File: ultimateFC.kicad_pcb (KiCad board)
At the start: 6 copper layers, 36 x 36 mm, 240 parts, among them J1 USB_B_Micro, SW1 SW_Push, U1 LMR33630CQRNX, U2 TPS62824ADMQ, U3 LMR33620CRNXT, U4 S25FL064L, U5 DPS310, U6 BMI270, U7 STM32H735VGH6, U8 ICM-20602, Y1 CSTNE8M00G550000R0

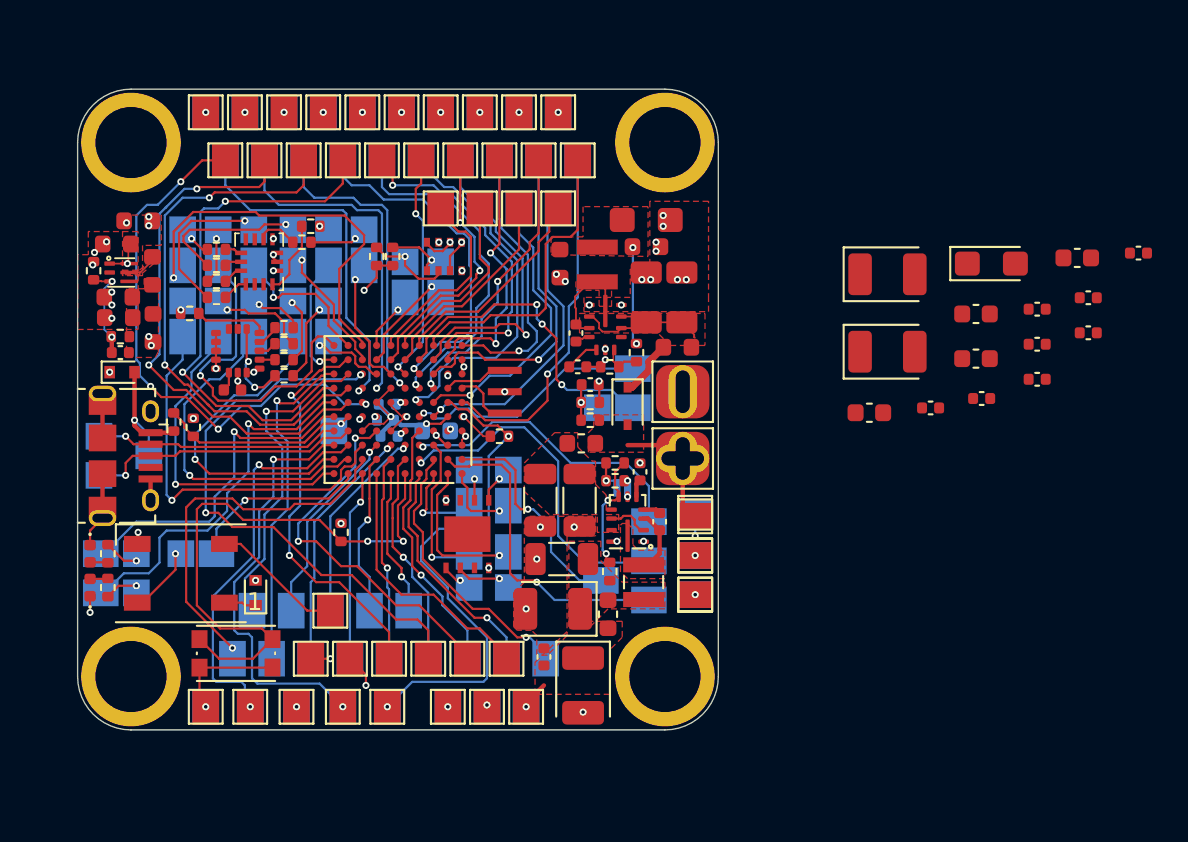
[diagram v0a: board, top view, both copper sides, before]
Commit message: add RF connectors
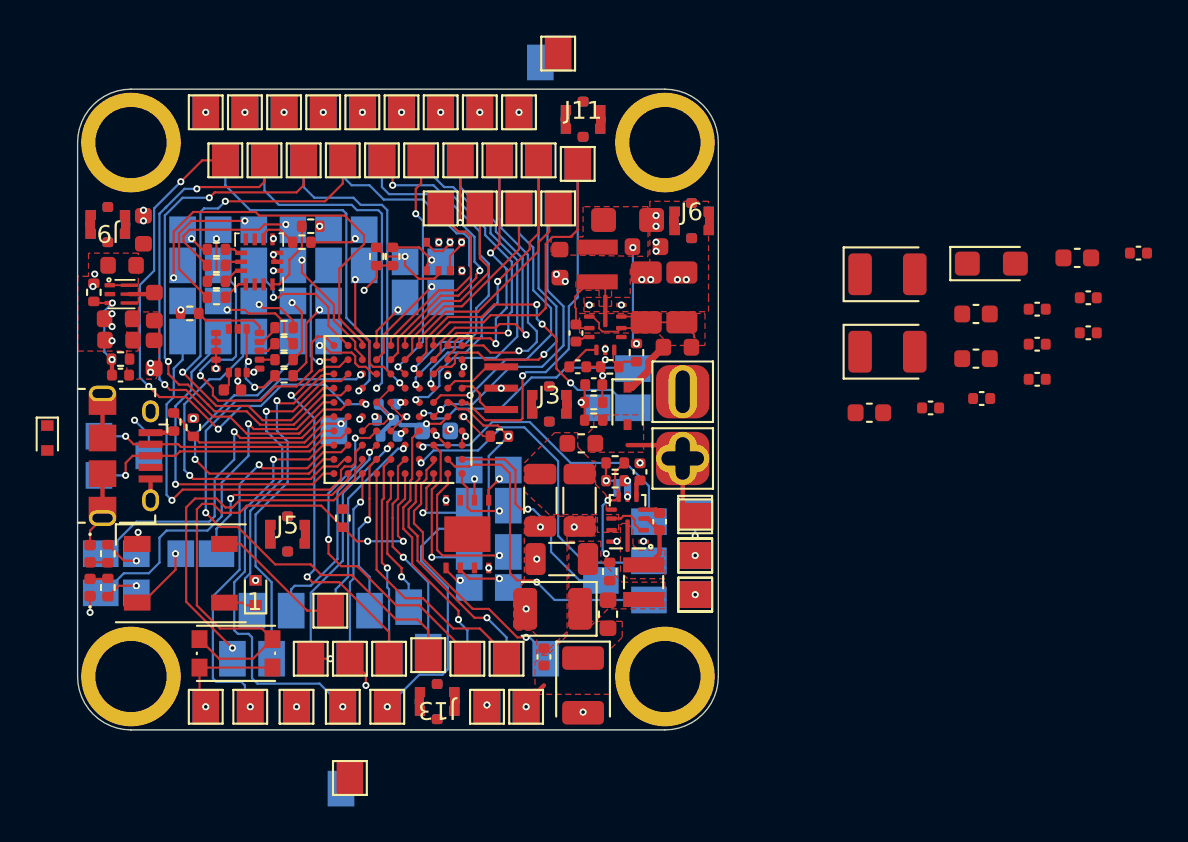
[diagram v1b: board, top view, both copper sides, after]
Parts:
- added J10: Conn_Coaxial, ultimateFC:Amphenol_RF_A-4JA, B.Cu at (125.4, 98.7)
- added J11: Conn_Coaxial, ultimateFC:Amphenol_RF_A-4JA, F.Cu at (125.4, 98.7)
- added J12: Conn_Coaxial, ultimateFC:Amphenol_RF_A-4JA, B.Cu at (117.2, 131.4)
- added J13: Conn_Coaxial, ultimateFC:Amphenol_RF_A-4JA, F.Cu at (117.2, 131.4)
- added J2: Conn_Coaxial, ultimateFC:Amphenol_RF_A-4JA, B.Cu at (123.5, 114.7)
- added J3: Conn_Coaxial, ultimateFC:Amphenol_RF_A-4JA, F.Cu at (123.5, 114.7)
- added J4: Conn_Coaxial, ultimateFC:Amphenol_RF_A-4JA, B.Cu at (108.8, 122.0)
- added J5: Conn_Coaxial, ultimateFC:Amphenol_RF_A-4JA, F.Cu at (108.8, 122.0)
- added J6: Conn_Coaxial, ultimateFC:Amphenol_RF_A-4JA, F.Cu at (131.5, 104.4)
- added J7: Conn_Coaxial, ultimateFC:Amphenol_RF_A-4JA, B.Cu at (131.5, 104.4)
- added J8: Conn_Coaxial, ultimateFC:Amphenol_RF_A-4JA, B.Cu at (98.7, 104.6)
- added J9: Conn_Coaxial, ultimateFC:Amphenol_RF_A-4JA, F.Cu at (98.7, 104.6)
- moved TP142 7.56 mm to (111.8, 136.3)
- moved TP28 6.80 mm to (112.3, 135.7)
- moved D4 5.60 mm to (95.3, 116.6), turned to -90 degrees
- moved TP126 3.30 mm to (124.0, 95.0)
- moved TP130 2.97 mm to (123.0, 95.5)
- moved L2 2.01 mm to (101.3, 109.2)
- moved FB4 1.49 mm to (101.3, 111.9)
- moved C26 1.27 mm to (99.3, 111.1)
- moved C23 1.27 mm to (99.4, 113.1)
- moved R3 1.27 mm to (99.4, 112.2)
- moved C11 1.24 mm to (99.5, 106.9)
- moved C24 1.22 mm to (99.3, 109.9)
- moved R4 1.22 mm to (97.9, 108.4)
- moved U2 1.22 mm to (99.5, 108.5)
- moved C6 1.05 mm to (127.9, 104.3)
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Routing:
- net USB_VBUS: track 7.73 -> 3.67 mm
- net /NRST: track 29.1 -> 25.7 mm
- net UART2_TX: track 20.9 -> 18.9 mm
- net Net-(C11-Pad1): track 1.96 -> 1.06 mm, vias 2 -> 0
- net ESC_4_TX: track 19.1 -> 19.8 mm
- net GND: track 19.5 -> 18.9 mm, vias 54 -> 51
- net Net-(TP51-Pad1): track 10.3 -> 10.8 mm
- net Net-(TP49-Pad1): track 11.3 -> 11.8 mm
- net +5V: vias 12 -> 10
- removed copper zone on F.Cu, net Net-(C11-Pad1)
- removed copper zone on F.Cu, net Net-(L2-Pad1)

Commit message: update layout
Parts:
- removed C10, C12, C13, C14, C15, C16, C17, C9: 4.7µF, Capacitor_SMD:C_0402_1005Metric
- removed C18, C19, C20, C21: 2.2µF, Capacitor_SMD:C_0603_1608Metric
- removed C22: 10µF, Capacitor_Tantalum_SMD:CP_EIA-3216-18_Kemet-A
- removed C7, C8: 220µF, Capacitor_Tantalum_SMD:CP_EIA-3528-15_AVX-H
- removed J10, J11, J12, J13, J6, J7: Conn_Coaxial, ultimateFC:Amphenol_RF_A-4JA
- moved J8 32.7 mm to (131.4, 104.6), turned to -90 degrees
- moved J9 32.7 mm to (131.4, 104.6), turned to 90 degrees
- moved TP142 7.56 mm to (117.8, 131.7)
- moved TP28 6.80 mm to (117.8, 131.7)
- moved D4 5.37 mm to (99.1, 112.8), turned to 0 degrees
- moved TP126 3.30 mm to (124.0, 98.3)
- moved TP130 2.97 mm to (124.0, 98.3)
- moved R11 2.22 mm to (113.2, 122.9), turned to -90 degrees
- moved C11 1.40 mm to (99.5, 105.5)
- moved C24 1.40 mm to (99.3, 108.5)
- moved FB4 1.40 mm to (101.3, 110.5)
- moved L2 1.40 mm to (101.3, 107.8)
- moved R3 1.40 mm to (99.4, 110.8)
- moved R4 1.40 mm to (97.9, 107.0)
- moved U2 1.40 mm to (99.5, 107.1)
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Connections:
- J4 pad 1: Net-(J5-Pad1) -> +5V
- J5 pad 1: Net-(J5-Pad1) -> +5V
- J8 pad 1: Net-(J8-Pad1) -> +3V3
- J9 pad 1: Net-(J8-Pad1) -> +3V3
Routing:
- net USB_VBUS: track 3.67 -> 7.01 mm
- net UART2_TX: track 18.9 -> 20.7 mm
- net UC_LED_1: track 18.7 -> 19.5 mm
- net Net-(TP75-Pad1): track 19.2 -> 18.5 mm
- net UART4_TX: track 16.0 -> 15.4 mm
- net Net-(TP74-Pad1): track 19.4 -> 18.8 mm
- net GND: track 18.9 -> 18.8 mm, vias 51 -> 62
- net Net-(J2-Pad1): vias 0 -> 1
- net +5V: vias 10 -> 13
- net +3V3: vias 18 -> 19
- added copper zone on F.Cu, net Net-(C11-Pad1)

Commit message: update layout
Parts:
- removed TP137, TP138, TP139, TP140, TP66: Pad, TestPoint:TestPoint_Pad_1.5x1.5mm
- added C39: 4.7µF, Capacitor_SMD:C_0603_1608Metric, F.Cu at (107.0, 125.1)
- SW1: footprint Button_Switch_SMD:SW_Push_1P1T_NO_CK_KMR2 -> Button_Switch_SMD:SW_Push_1P1T-SH_NO_CK_KMR2xxG
- TP141, TP65, TP67, TP88, TP89: footprint TestPoint:TestPoint_Pad_1.5x1.5mm -> ultimateFC:chonker_swd_pad
- moved D6 1.43 mm to (108.4, 125.6)
- moved R17 1.32 mm to (109.8, 104.3)
- moved R7 1.02 mm to (114.8, 106.6), turned to -90 degrees
- moved R8 1.02 mm to (115.7, 106.6), turned to -90 degrees
- moved R16 0.85 mm to (109.8, 105.5)
- moved D4 0.80 mm to (98.3, 112.8)
- moved J4 0.50 mm to (108.5, 122.4)
- moved J5 0.50 mm to (108.5, 122.4)
- moved SW1 0.40 mm to (105.9, 128.3)
- moved C27 0.32 mm to (125.1, 120.4)
- moved C28 0.30 mm to (123.0, 120.4)
- moved TP116 0.30 mm to (112.3, 128.7)
- moved TP36 0.30 mm to (114.5, 128.7)
- moved TP39 0.30 mm to (118.9, 128.7)
- moved TP40 0.30 mm to (116.7, 128.7)
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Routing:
- net UART3_RX: track 31.8 -> 36.1 mm
- net Net-(R11-Pad1): track 32.5 -> 28.7 mm
- net Net-(TP102-Pad1): track 17.9 -> 20.3 mm
- net /INT2_270: track 2.57 -> 4.70 mm
- net /SCL_DPS: track 4.82 -> 2.81 mm
- net Net-(TP50-Pad1): track 20.4 -> 22.4 mm
- net CS_OSD: track 21.6 -> 20.0 mm
- net /SCK_DPS: track 3.21 -> 1.68 mm
- net Net-(D5-Pad1): track 1.81 -> 3.34 mm
- net SCLK_GYRO: track 19.5 -> 20.8 mm
- net Net-(R16-Pad2): track 4.18 -> 3.24 mm
- net MISO_GYRO: track 19.3 -> 20.2 mm
- net MOSI_GYRO: track 18.4 -> 19.3 mm
- net Net-(TP49-Pad1): track 11.8 -> 11.0 mm
- net SCLK_OSD: track 7.01 -> 6.18 mm
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
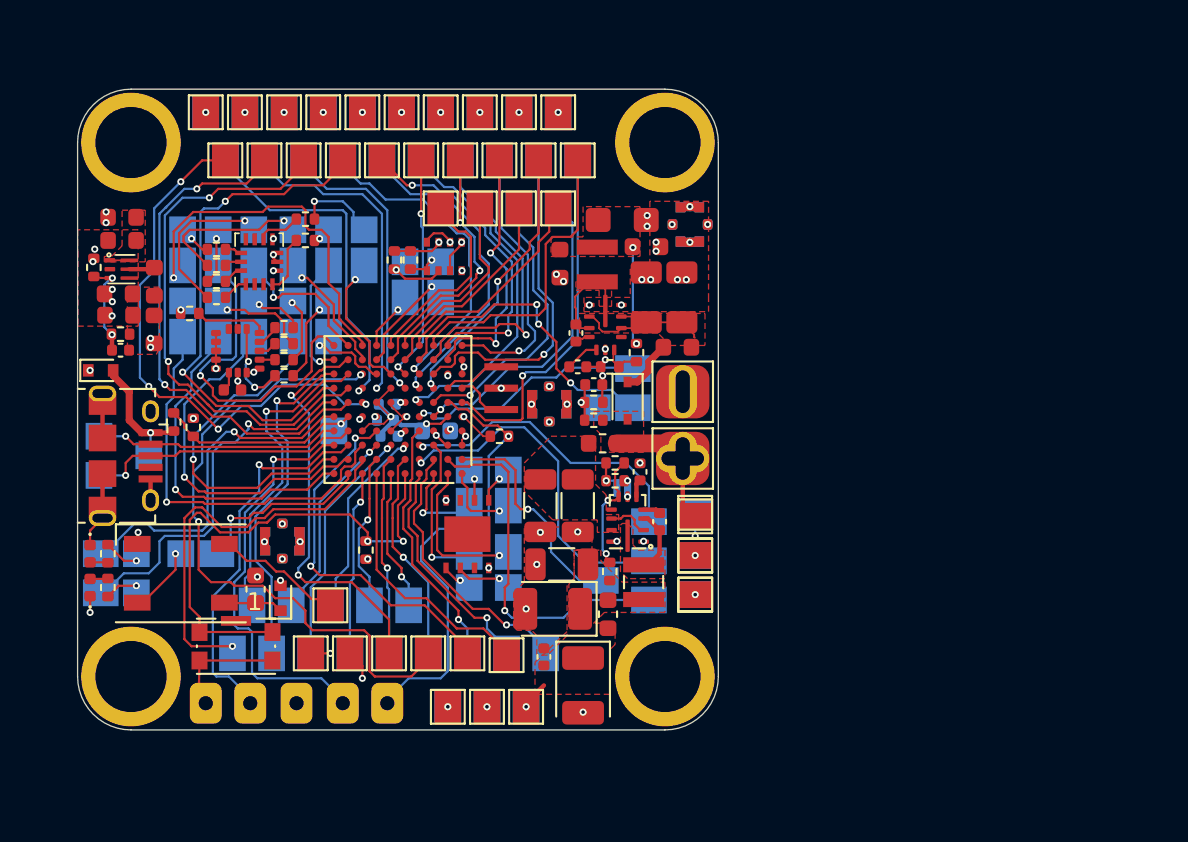
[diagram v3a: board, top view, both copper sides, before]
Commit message: change pads, add coax datasheet
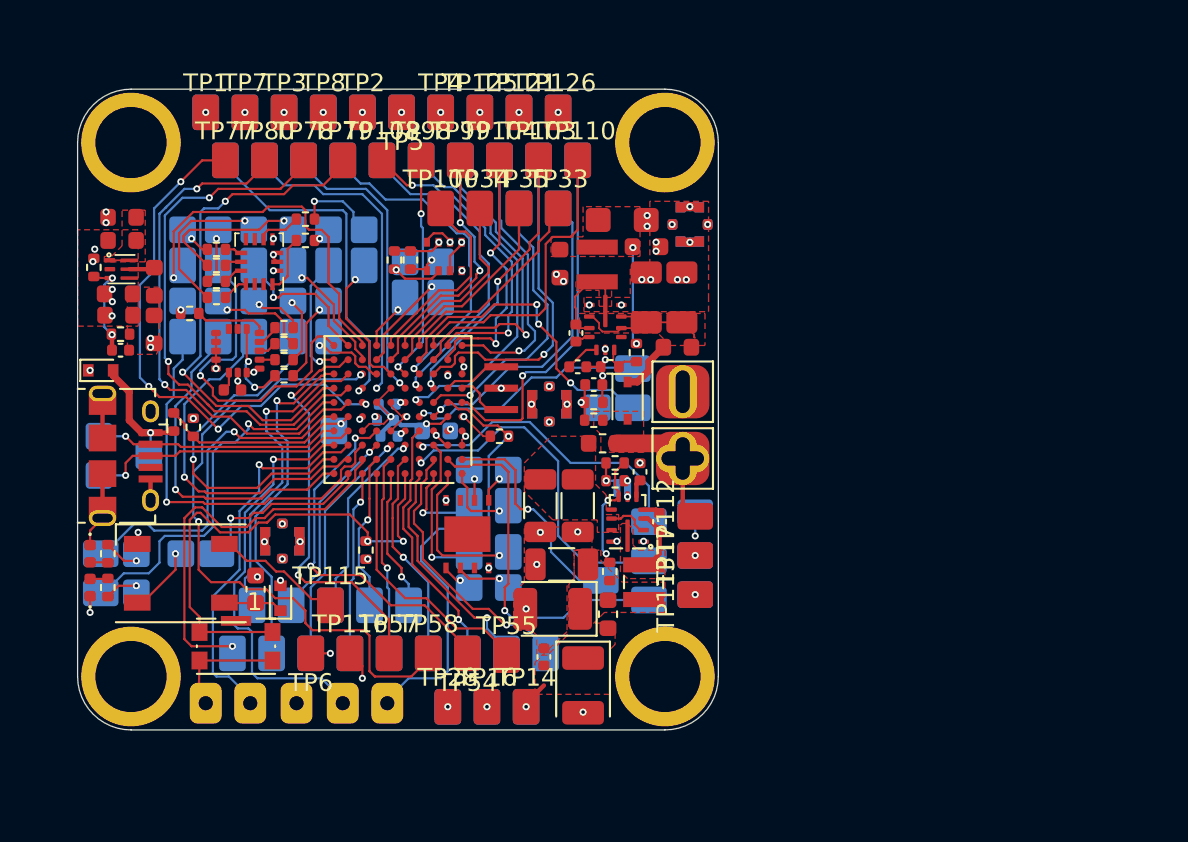
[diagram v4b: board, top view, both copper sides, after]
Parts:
- TP1, TP100, TP101, TP102, TP103, TP104, TP105, TP106, TP107, TP108, TP109, TP110, TP112, TP113, TP115, TP116, TP121, TP122, TP123, TP124, TP125, TP126, TP127, TP128, TP129, TP130, TP131, TP132, TP133, TP14, TP142, TP143, TP15, TP16, TP17, TP2, TP28, TP3, TP33, TP34, TP35, TP36, TP37, TP38, TP39, TP4, TP40, TP41, TP42, TP43, TP44, TP45, TP46, TP47, TP48, TP49, TP5, TP50, TP51, TP52, TP53, TP54, TP55, TP56, TP57, TP58, TP59, TP6, TP60, TP61, TP62, TP63, TP64, TP7, TP71, TP72, TP73, TP74, TP75, TP76, TP77, TP78, TP79, TP8, TP80, TP81, TP82, TP83, TP84, TP85, TP86, TP87, TP90, TP91, TP92, TP93, TP94, TP95, TP96, TP97, TP98, TP99: footprint TestPoint:TestPoint_Pad_1.5x1.5mm -> ultimateFC:chonker_TestPoint_Pad_1.5x2.0mm
- TP10, TP11, TP114, TP117, TP118, TP119, TP12, TP120, TP13, TP18, TP19, TP22, TP23, TP24, TP25, TP26, TP27, TP29, TP30, TP31, TP32, TP68, TP69, TP70, TP9: footprint TestPoint:TestPoint_Pad_1.5x1.5mm -> ultimateFC:chonker_TestPoint_Pad_1.5x1.5mm
- TP134, TP135, TP136: footprint TestPoint:TestPoint_Pad_1.5x1.5mm -> ultimateFC:chonker_TestPoint_Pad_1.5x2.0mm; moved to B.Cu

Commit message: update layout
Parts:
- TP141: moved to F.Cu
- TP65, TP67, TP88, TP89: moved to B.Cu
- turned TP141 to 0 degrees
- turned TP65 to 180 degrees
- turned TP67 to 180 degrees
- turned TP88 to 180 degrees
- turned TP89 to 180 degrees

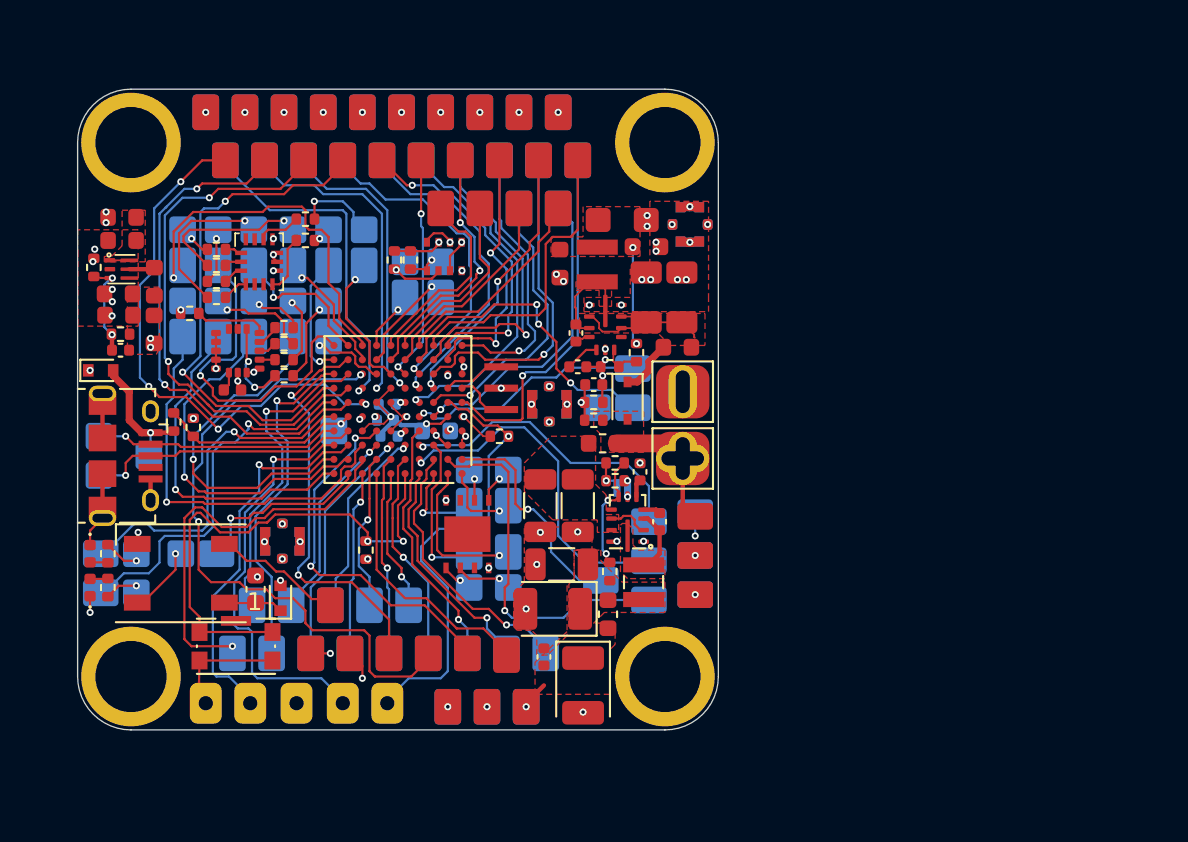
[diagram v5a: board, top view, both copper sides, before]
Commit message: Added Caps
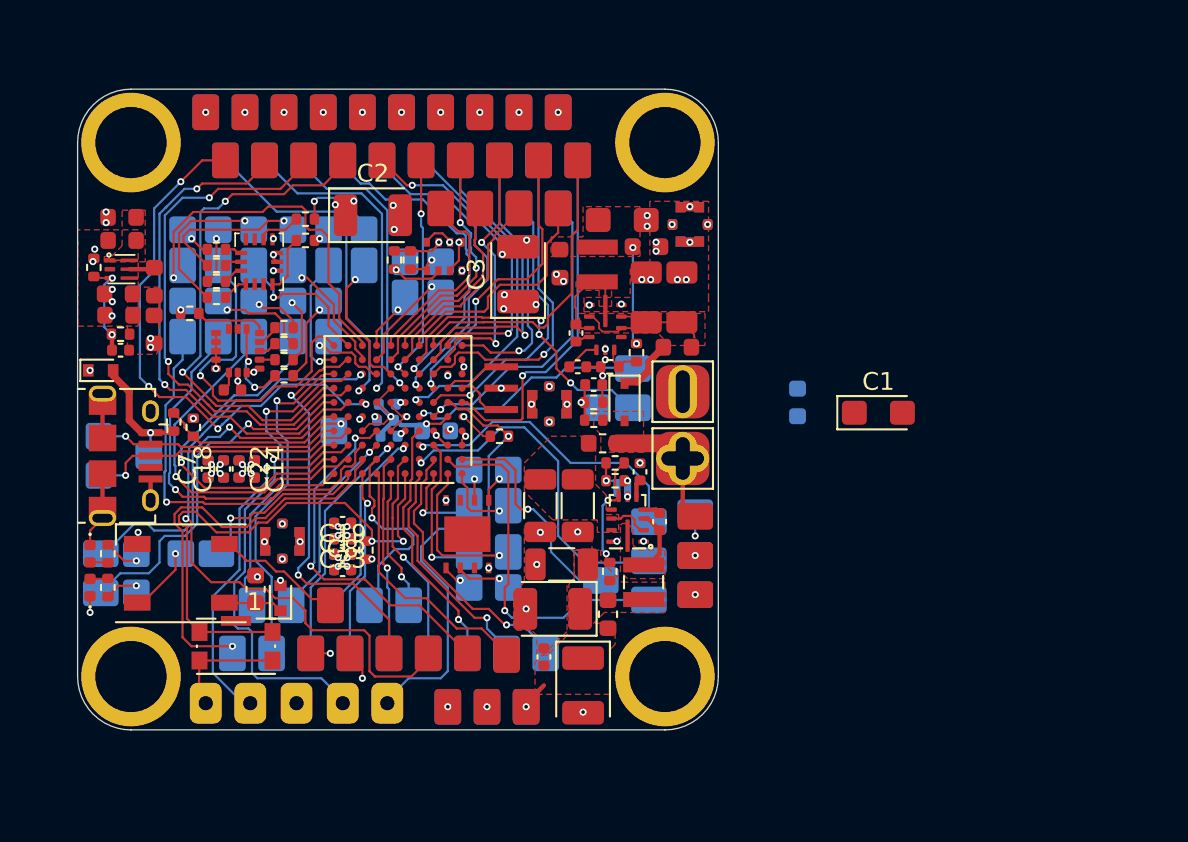
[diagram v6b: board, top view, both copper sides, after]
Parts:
- added C1: 10µF, Capacitor_Tantalum_SMD:CP_EIA-3216-18_Kemet-A, F.Cu at (142.0, 115.2)
- added C10: 2.2µF, Capacitor_SMD:C_0603_1608Metric, B.Cu at (137.4, 114.6)
- added C12: 4.7µF, Capacitor_SMD:C_0402_1005Metric, B.Cu at (104.3, 118.3)
- added C13: 4.7µF, Capacitor_SMD:C_0402_1005Metric, B.Cu at (111.9, 121.4)
- added C14: 4.7µF, Capacitor_SMD:C_0402_1005Metric, F.Cu at (106.9, 118.3)
- added C15: 4.7µF, Capacitor_SMD:C_0402_1005Metric, F.Cu at (111.9, 121.4)
- added C16: 4.7µF, Capacitor_SMD:C_0402_1005Metric, B.Cu at (106.1, 118.3)
- added C17: 4.7µF, Capacitor_SMD:C_0402_1005Metric, B.Cu at (111.9, 124.0)
- added C18: 4.7µF, Capacitor_SMD:C_0402_1005Metric, F.Cu at (105.2, 118.3)
- added C19: 4.7µF, Capacitor_SMD:C_0402_1005Metric, F.Cu at (111.9, 123.1)
- added C2: 220µF, Capacitor_Tantalum_SMD:CP_EIA-3528-15_AVX-H, F.Cu at (113.6, 104.1)
- added C20: 4.7µF, Capacitor_SMD:C_0402_1005Metric, B.Cu at (106.9, 118.3)
- added C21: 4.7µF, Capacitor_SMD:C_0402_1005Metric, B.Cu at (111.9, 122.3)
- added C22: 4.7µF, Capacitor_SMD:C_0402_1005Metric, F.Cu at (106.1, 118.3)
- added C23: 4.7µF, Capacitor_SMD:C_0402_1005Metric, F.Cu at (111.9, 122.3)
- added C3: 220µF, Capacitor_Tantalum_SMD:CP_EIA-3528-15_AVX-H, F.Cu at (121.8, 107.4)
- added C5: 4.7µF, Capacitor_SMD:C_0402_1005Metric, B.Cu at (105.2, 118.3)
- added C6: 4.7µF, Capacitor_SMD:C_0402_1005Metric, B.Cu at (111.9, 123.1)
- added C7: 4.7µF, Capacitor_SMD:C_0402_1005Metric, F.Cu at (104.3, 118.3)
- added C8: 4.7µF, Capacitor_SMD:C_0402_1005Metric, F.Cu at (111.9, 124.0)
- moved D1 0.19 mm to (127.7, 114.6)
- renumbered C3 to C11, C4 to C24, C5 to C25, C6 to C26, C11 to C27, C23 to C28, C24 to C29, C25 to C30, C26 to C31, C27 to C32, C28 to C33, C29 to C34, C30 to C35, C31 to C36, C32 to C37, C33 to C38, C34 to C39, C1 to C4, C39 to C40, C35 to C41, C36 to C42, C37 to C43, C38 to C44, C2 to C9, D6 to D2, D5 to D3, D2 to D4, D3 to D5, D4 to D6, J2 to J1, J3 to J2, J4 to J3, J5 to J4, J8 to J5, J9 to J6, J1 to J7, R28 to R11, R11 to R12, R22 to R13, R18 to R14, R19 to R15, R20 to R16, R21 to R17, R12 to R18, R13 to R19, R14 to R20, R15 to R21, R16 to R22, R17 to R23, R23 to R24, R24 to R25, R25 to R26, R26 to R27, R27 to R28, TP5 to TP1, TP130 to TP10, TP78 to TP100, TP79 to TP101, TP80 to TP102, TP81 to TP103, TP82 to TP104, TP83 to TP105, TP84 to TP106, TP85 to TP107, TP86 to TP108, TP87 to TP109, TP131 to TP11, TP88 to TP110, TP89 to TP111, TP90 to TP112, TP91 to TP113, TP92 to TP114, TP93 to TP115, TP94 to TP116, TP95 to TP117, TP96 to TP118, TP97 to TP119, TP134 to TP12, TP98 to TP120, TP99 to TP121, TP100 to TP122, TP101 to TP123, TP102 to TP124, TP103 to TP125, TP104 to TP126, TP105 to TP127, TP106 to TP128, TP107 to TP129, TP143 to TP13, TP108 to TP130, TP109 to TP131, TP110 to TP132, TP69 to TP133, TP70 to TP134, TP117 to TP135, TP119 to TP136, TP120 to TP137, TP118 to TP138, TP142 to TP14, TP135 to TP15, TP132 to TP16, TP133 to TP17, TP121 to TP18, TP122 to TP19, TP6 to TP2, TP116 to TP20, TP113 to TP21, TP28 to TP22, TP1 to TP23, TP2 to TP24, TP141 to TP25, TP136 to TP26, TP129 to TP27, TP123 to TP28, TP3 to TP29, TP7 to TP3, TP4 to TP30, TP9 to TP31, TP10 to TP32, TP11 to TP33, TP12 to TP34, TP13 to TP35, TP111 to TP36, TP114 to TP37, TP14 to TP38, TP15 to TP39, TP8 to TP4, TP16 to TP40, TP17 to TP41, TP115 to TP42, TP18 to TP43, TP19 to TP44, TP29 to TP45, TP30 to TP46, TP31 to TP47, TP32 to TP48, TP22 to TP49, TP124 to TP5, TP23 to TP50, TP24 to TP51, TP25 to TP52, TP26 to TP53, TP27 to TP54, TP65 to TP55, TP33 to TP56, TP34 to TP57, TP35 to TP58, TP36 to TP59, TP125 to TP6, TP37 to TP60, TP38 to TP61, TP39 to TP62, TP40 to TP63, TP41 to TP64, TP42 to TP65, TP43 to TP66, TP44 to TP67, TP45 to TP68, TP46 to TP69, TP126 to TP7, TP47 to TP70, TP48 to TP71, TP49 to TP72, TP50 to TP73, TP51 to TP74, TP52 to TP75, TP53 to TP76, TP54 to TP77, TP55 to TP78, TP56 to TP79, TP127 to TP8, TP57 to TP80, TP58 to TP81, TP59 to TP82, TP60 to TP83, TP61 to TP84, TP62 to TP85, TP63 to TP86, TP64 to TP87, TP67 to TP88, TP112 to TP89, TP128 to TP9, TP20 to TP90, TP21 to TP91, TP68 to TP92, TP71 to TP93, TP72 to TP94, TP73 to TP95, TP74 to TP96, TP75 to TP97, TP76 to TP98, TP77 to TP99, U7 to U6, U8 to U7, U6 to U8
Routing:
- net Net-(TP76-Pad1): track 8.86 -> 11.8 mm
- net MP_PIN1: track 12.0 -> 14.1 mm
- net Net-(R12-Pad1): track 28.7 -> 30.4 mm
- net UART4_TX: track 15.4 -> 16.5 mm
- net Net-(TP73-Pad1): track 22.4 -> 23.3 mm
- net vol_sig: track 17.6 -> 16.7 mm
- net SWDCLK: track 21.4 -> 20.7 mm
- net SCLK_GYRO: track 20.8 -> 21.4 mm
- net +3V3: vias 17 -> 24
- net GND: vias 62 -> 74
- net +5V: vias 13 -> 19
- added copper zone on F.Cu, net Net-(C11-Pad1)
- added copper zone on F.Cu, net Net-(C30-Pad1)
- removed copper zone on F.Cu, net Net-(C24-Pad1)
- removed copper zone on F.Cu, net Net-(C32-Pad1)
- removed copper zone on F.Cu, net Net-(C35-Pad1)

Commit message: add caps
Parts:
- C1: moved to B.Cu
- moved C1 15.2 mm to (126.9, 116.5), turned to 180 degrees
- moved C10 11.1 mm to (126.9, 118.0), turned to 180 degrees
- moved TP31 0.30 mm to (126.2, 114.6)
- moved TP98 0.30 mm to (128.2, 114.6)
- moved TP106 0.30 mm to (128.2, 112.4)
- moved TP36 0.10 mm to (127.6, 119.5)
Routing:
- net +BATT: track 7.60 -> 11.2 mm, vias 0 -> 3
- net Net-(C27-Pad1): track 1.06 -> 2.33 mm
- net ESC_1_TX: track 17.3 -> 18.1 mm, vias 0 -> 2
- net GND: vias 74 -> 77
- added copper zone on B.Cu, net +BATT
- added copper zone on B.Cu, net GND
- added copper zone on F.Cu, net Net-(C32-Pad1)
- added copper zone on F.Cu, net Net-(C35-Pad1)
- removed copper zone on F.Cu, net Net-(C11-Pad1)
- removed copper zone on F.Cu, net Net-(C30-Pad1)
